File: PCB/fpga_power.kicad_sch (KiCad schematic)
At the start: 11 parts, among them U2 LFE5U-25F-6BG256C

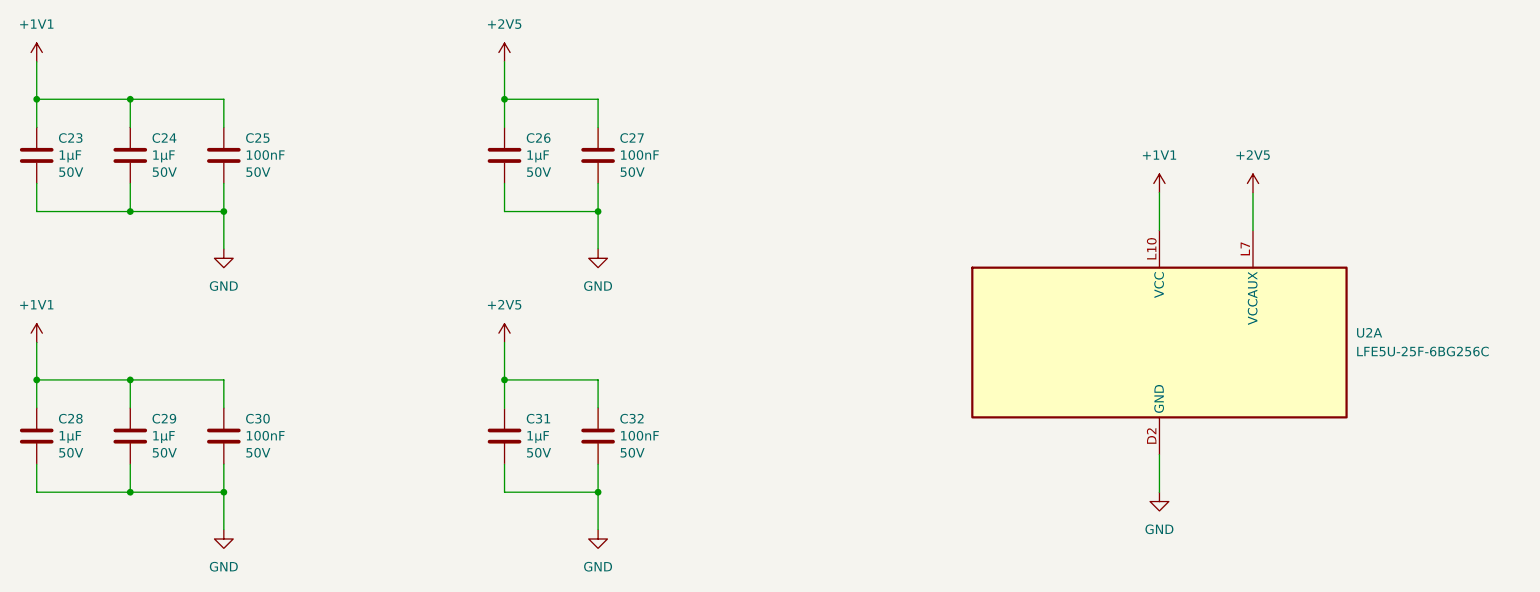
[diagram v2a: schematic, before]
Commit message: Add the USB to JTAG bridge
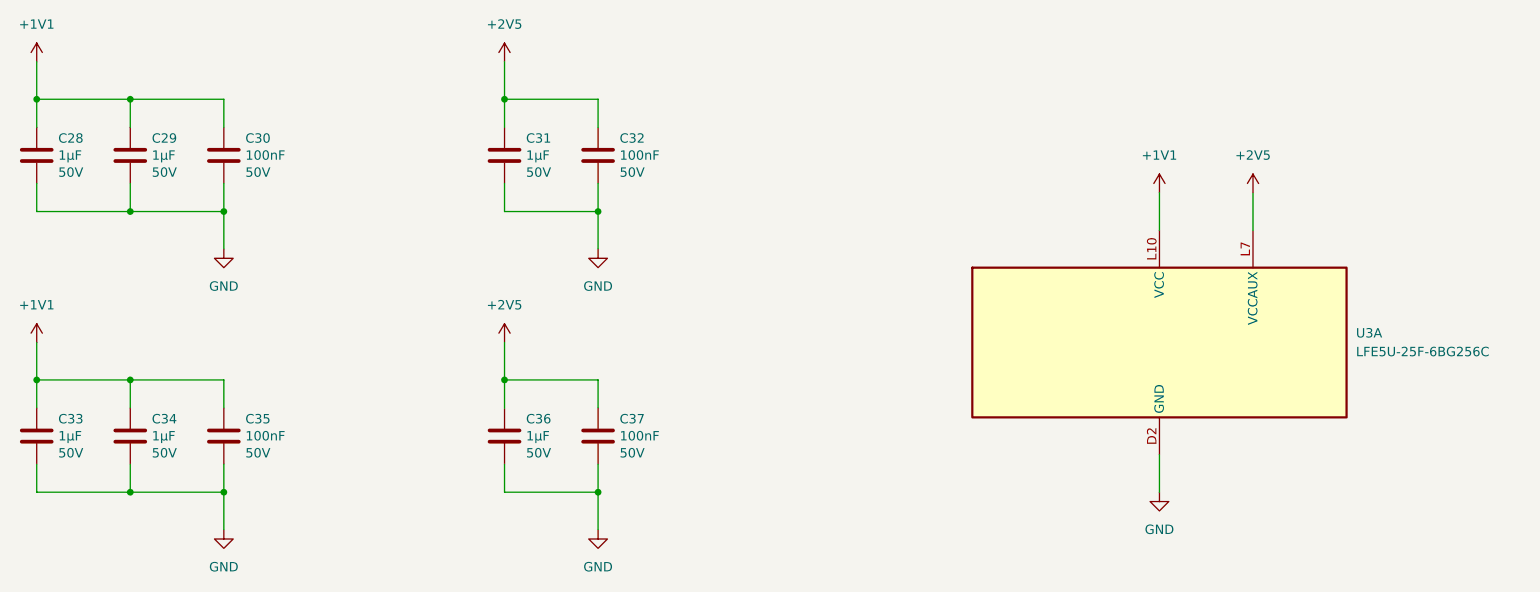
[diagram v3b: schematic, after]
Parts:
- renumbered C23 to C28, C24 to C29, C25 to C30, C26 to C31, C27 to C32, C28 to C33, C29 to C34, C30 to C35, C31 to C36, C32 to C37, U2 to U3
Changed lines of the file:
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@@
 		(on_board yes)
 		(dnp no)
-		(property "Reference" "C23"
+		(property "Reference" "C28"
 			(at 53.721 61.1886 0)
 			(effects
@@
 			(project "clavier"
 				(path "/6362c6e0-59ef-40d3-b6e0-7e9dfe7b9b20/d73938da-f0ba-48e3-aac9-a36988c25c2c/e36c52fe-7af8-49a0-bf3c-a636c30fc9cb"
-					(reference "C23")
+					(reference "C28")
 					(unit 1)
 				)
@@
 		(on_board yes)
 		(dnp no)
-		(property "Reference" "C25"
+		(property "Reference" "C30"
 			(at 79.121 61.1886 0)
 			(effects
@@
 			(project "clavier"
 				(path "/6362c6e0-59ef-40d3-b6e0-7e9dfe7b9b20/d73938da-f0ba-48e3-aac9-a36988c25c2c/e36c52fe-7af8-49a0-bf3c-a636c30fc9cb"
-					(reference "C25")
+					(reference "C30")
 					(unit 1)
 				)
@@
 		(on_board yes)
 		(dnp no)
-		(property "Reference" "C24"
+		(property "Reference" "C29"
 			(at 66.421 61.1886 0)
 			(effects
@@
 			(project "clavier"
 				(path "/6362c6e0-59ef-40d3-b6e0-7e9dfe7b9b20/d73938da-f0ba-48e3-aac9-a36988c25c2c/e36c52fe-7af8-49a0-bf3c-a636c30fc9cb"
-					(reference "C24")
+					(reference "C29")
 					(unit 1)
 				)
@@
 		(on_board yes)
 		(dnp no)
-		(property "Reference" "C29"
+		(property "Reference" "C34"
 			(at 66.421 99.2886 0)
 			(effects
@@
 			(project "clavier"
 				(path "/6362c6e0-59ef-40d3-b6e0-7e9dfe7b9b20/d73938da-f0ba-48e3-aac9-a36988c25c2c/e36c52fe-7af8-49a0-bf3c-a636c30fc9cb"
-					(reference "C29")
+					(reference "C34")
 					(unit 1)
 				)
@@
 		(on_board yes)
 		(dnp no)
-		(property "Reference" "C31"
+		(property "Reference" "C36"
 			(at 117.221 99.2886 0)
 			(effects
@@
 			(project "clavier"
 				(path "/6362c6e0-59ef-40d3-b6e0-7e9dfe7b9b20/d73938da-f0ba-48e3-aac9-a36988c25c2c/e36c52fe-7af8-49a0-bf3c-a636c30fc9cb"
-					(reference "C31")
+					(reference "C36")
 					(unit 1)
 				)
@@
 		(on_board yes)
 		(dnp no)
-		(property "Reference" "C26"
+		(property "Reference" "C31"
 			(at 117.221 61.1886 0)
 			(effects
@@
 			(project "clavier"
 				(path "/6362c6e0-59ef-40d3-b6e0-7e9dfe7b9b20/d73938da-f0ba-48e3-aac9-a36988c25c2c/e36c52fe-7af8-49a0-bf3c-a636c30fc9cb"
-					(reference "C26")
+					(reference "C31")
 					(unit 1)
 				)
@@
 		(dnp no)
 		(fields_autoplaced yes)
-		(property "Reference" "U2"
+		(property "Reference" "U3"
 			(at 229.87 87.6299 0)
 			(effects
@@
 			(project "clavier"
 				(path "/6362c6e0-59ef-40d3-b6e0-7e9dfe7b9b20/d73938da-f0ba-48e3-aac9-a36988c25c2c/e36c52fe-7af8-49a0-bf3c-a636c30fc9cb"
-					(reference "U2")
+					(reference "U3")
 					(unit 1)
 				)
@@
 		(dnp no)
 		(fields_autoplaced yes)
-		(property "Reference" "#PWR044"
+		(property "Reference" "#PWR054"
 			(at 114.3 54.61 0)
 			(effects
@@
 			(project "clavier"
 				(path "/6362c6e0-59ef-40d3-b6e0-7e9dfe7b9b20/d73938da-f0ba-48e3-aac9-a36988c25c2c/e36c52fe-7af8-49a0-bf3c-a636c30fc9cb"
-					(reference "#PWR044")
+					(reference "#PWR054")
 					(unit 1)
 				)
@@
 		(on_board yes)
 		(dnp no)
-		(property "Reference" "C32"
+		(property "Reference" "C37"
 			(at 129.921 99.2886 0)
 			(effects
@@
 			(project "clavier"
 				(path "/6362c6e0-59ef-40d3-b6e0-7e9dfe7b9b20/d73938da-f0ba-48e3-aac9-a36988c25c2c/e36c52fe-7af8-49a0-bf3c-a636c30fc9cb"
-					(reference "C32")
+					(reference "C37")
 					(unit 1)
 				)
@@
 		(dnp no)
 		(fields_autoplaced yes)
-		(property "Reference" "#PWR053"
+		(property "Reference" "#PWR063"
 			(at 127 120.65 0)
 			(effects
@@
 			(project "clavier"
 				(path "/6362c6e0-59ef-40d3-b6e0-7e9dfe7b9b20/d73938da-f0ba-48e3-aac9-a36988c25c2c/e36c52fe-7af8-49a0-bf3c-a636c30fc9cb"
-					(reference "#PWR053")
+					(reference "#PWR063")
 					(unit 1)
 				)
@@
 		(dnp no)
 		(fields_autoplaced yes)
-		(property "Reference" "#PWR046"
+		(property "Reference" "#PWR056"
 			(at 215.9 72.39 0)
 			(effects
@@
 			(project "clavier"
 				(path "/6362c6e0-59ef-40d3-b6e0-7e9dfe7b9b20/d73938da-f0ba-48e3-aac9-a36988c25c2c/e36c52fe-7af8-49a0-bf3c-a636c30fc9cb"
-					(reference "#PWR046")
+					(reference "#PWR056")
 					(unit 1)
 				)
@@
 		(dnp no)
 		(fields_autoplaced yes)
-		(property "Reference" "#PWR045"
+		(property "Reference" "#PWR055"
 			(at 203.2 72.39 0)
 			(effects
@@
 			(project "clavier"
 				(path "/6362c6e0-59ef-40d3-b6e0-7e9dfe7b9b20/d73938da-f0ba-48e3-aac9-a36988c25c2c/e36c52fe-7af8-49a0-bf3c-a636c30fc9cb"
-					(reference "#PWR045")
+					(reference "#PWR055")
 					(unit 1)
 				)
@@
 		(dnp no)
 		(fields_autoplaced yes)
-		(property "Reference" "#PWR048"
+		(property "Reference" "#PWR058"
 			(at 127 82.55 0)
 			(effects
@@
 			(project "clavier"
 				(path "/6362c6e0-59ef-40d3-b6e0-7e9dfe7b9b20/d73938da-f0ba-48e3-aac9-a36988c25c2c/e36c52fe-7af8-49a0-bf3c-a636c30fc9cb"
-					(reference "#PWR048")
+					(reference "#PWR058")
 					(unit 1)
 				)
@@
 		(dnp no)
 		(fields_autoplaced yes)
-		(property "Reference" "#PWR047"
+		(property "Reference" "#PWR057"
 			(at 76.2 82.55 0)
 			(effects
@@
 			(project "clavier"
 				(path "/6362c6e0-59ef-40d3-b6e0-7e9dfe7b9b20/d73938da-f0ba-48e3-aac9-a36988c25c2c/e36c52fe-7af8-49a0-bf3c-a636c30fc9cb"
-					(reference "#PWR047")
+					(reference "#PWR057")
 					(unit 1)
 				)
@@
 		(dnp no)
 		(fields_autoplaced yes)
-		(property "Reference" "#PWR043"
+		(property "Reference" "#PWR053"
 			(at 50.8 54.61 0)
 			(effects
@@
 			(project "clavier"
 				(path "/6362c6e0-59ef-40d3-b6e0-7e9dfe7b9b20/d73938da-f0ba-48e3-aac9-a36988c25c2c/e36c52fe-7af8-49a0-bf3c-a636c30fc9cb"
-					(reference "#PWR043")
+					(reference "#PWR053")
 					(unit 1)
 				)
@@
 		(on_board yes)
 		(dnp no)
-		(property "Reference" "C28"
+		(property "Reference" "C33"
 			(at 53.721 99.2886 0)
 			(effects
@@
 			(project "clavier"
 				(path "/6362c6e0-59ef-40d3-b6e0-7e9dfe7b9b20/d73938da-f0ba-48e3-aac9-a36988c25c2c/e36c52fe-7af8-49a0-bf3c-a636c30fc9cb"
-					(reference "C28")
+					(reference "C33")
 					(unit 1)
 				)
@@
 		(dnp no)
 		(fields_autoplaced yes)
-		(property "Reference" "#PWR051"
+		(property "Reference" "#PWR061"
 			(at 203.2 115.57 0)
 			(effects
@@
 			(project "clavier"
 				(path "/6362c6e0-59ef-40d3-b6e0-7e9dfe7b9b20/d73938da-f0ba-48e3-aac9-a36988c25c2c/e36c52fe-7af8-49a0-bf3c-a636c30fc9cb"
-					(reference "#PWR051")
+					(reference "#PWR061")
 					(unit 1)
 				)
@@
 		(dnp no)
 		(fields_autoplaced yes)
-		(property "Reference" "#PWR049"
+		(property "Reference" "#PWR059"
 			(at 50.8 92.71 0)
 			(effects
@@
 			(project "clavier"
 				(path "/6362c6e0-59ef-40d3-b6e0-7e9dfe7b9b20/d73938da-f0ba-48e3-aac9-a36988c25c2c/e36c52fe-7af8-49a0-bf3c-a636c30fc9cb"
-					(reference "#PWR049")
+					(reference "#PWR059")
 					(unit 1)
 				)
@@
 		(on_board yes)
 		(dnp no)
-		(property "Reference" "C27"
+		(property "Reference" "C32"
 			(at 129.921 61.1886 0)
 			(effects
@@
 			(project "clavier"
 				(path "/6362c6e0-59ef-40d3-b6e0-7e9dfe7b9b20/d73938da-f0ba-48e3-aac9-a36988c25c2c/e36c52fe-7af8-49a0-bf3c-a636c30fc9cb"
-					(reference "C27")
+					(reference "C32")
 					(unit 1)
 				)
@@
 		(dnp no)
 		(fields_autoplaced yes)
-		(property "Reference" "#PWR050"
+		(property "Reference" "#PWR060"
 			(at 114.3 92.71 0)
 			(effects
@@
 			(project "clavier"
 				(path "/6362c6e0-59ef-40d3-b6e0-7e9dfe7b9b20/d73938da-f0ba-48e3-aac9-a36988c25c2c/e36c52fe-7af8-49a0-bf3c-a636c30fc9cb"
-					(reference "#PWR050")
+					(reference "#PWR060")
 					(unit 1)
 				)
@@
 		(dnp no)
 		(fields_autoplaced yes)
-		(property "Reference" "#PWR052"
+		(property "Reference" "#PWR062"
 			(at 76.2 120.65 0)
 			(effects
@@
 			(project "clavier"
 				(path "/6362c6e0-59ef-40d3-b6e0-7e9dfe7b9b20/d73938da-f0ba-48e3-aac9-a36988c25c2c/e36c52fe-7af8-49a0-bf3c-a636c30fc9cb"
-					(reference "#PWR052")
+					(reference "#PWR062")
 					(unit 1)
 				)
@@
 		(on_board yes)
 		(dnp no)
-		(property "Reference" "C30"
+		(property "Reference" "C35"
 			(at 79.121 99.2886 0)
 			(effects
@@
 			(project "clavier"
 				(path "/6362c6e0-59ef-40d3-b6e0-7e9dfe7b9b20/d73938da-f0ba-48e3-aac9-a36988c25c2c/e36c52fe-7af8-49a0-bf3c-a636c30fc9cb"
-					(reference "C30")
+					(reference "C35")
 					(unit 1)
 				)

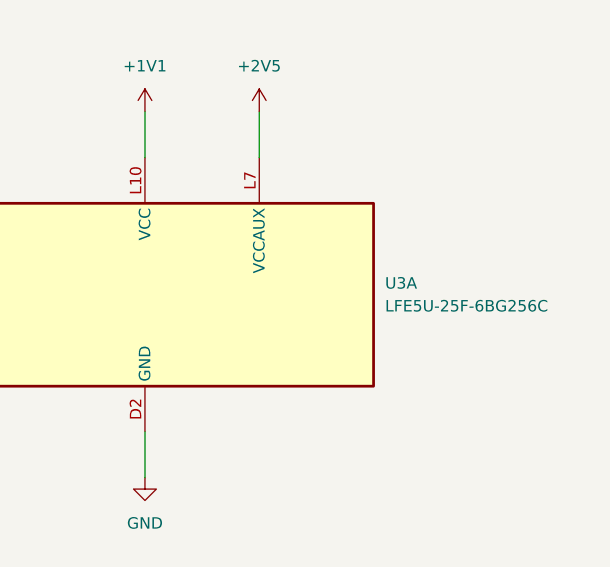
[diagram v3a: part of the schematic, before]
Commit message: Improve the CH347F schematics and added 3D models
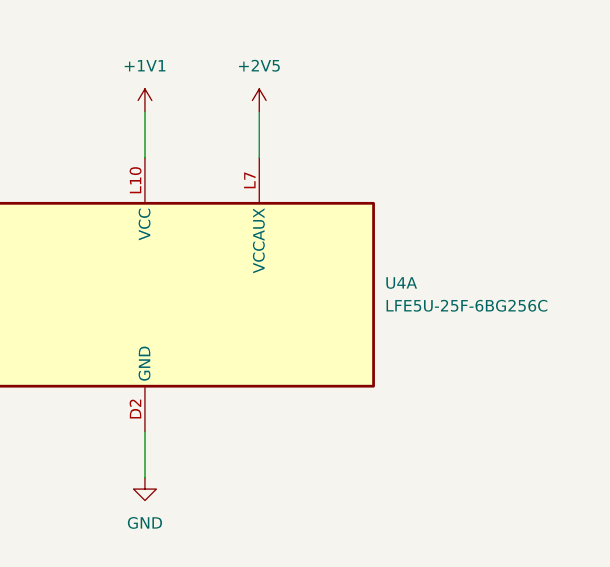
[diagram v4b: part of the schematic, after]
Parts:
- renumbered U3 to U4
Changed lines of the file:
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@@
 		(dnp no)
 		(fields_autoplaced yes)
-		(property "Reference" "U3"
+		(property "Reference" "U4"
 			(at 229.87 87.6299 0)
 			(effects
@@
 			(project "clavier"
 				(path "/6362c6e0-59ef-40d3-b6e0-7e9dfe7b9b20/d73938da-f0ba-48e3-aac9-a36988c25c2c/e36c52fe-7af8-49a0-bf3c-a636c30fc9cb"
-					(reference "U3")
+					(reference "U4")
 					(unit 1)
 				)
@@
 		(dnp no)
 		(fields_autoplaced yes)
-		(property "Reference" "#PWR054"
+		(property "Reference" "#PWR058"
 			(at 114.3 54.61 0)
 			(effects
@@
 			(project "clavier"
 				(path "/6362c6e0-59ef-40d3-b6e0-7e9dfe7b9b20/d73938da-f0ba-48e3-aac9-a36988c25c2c/e36c52fe-7af8-49a0-bf3c-a636c30fc9cb"
-					(reference "#PWR054")
+					(reference "#PWR058")
 					(unit 1)
 				)
@@
 		(dnp no)
 		(fields_autoplaced yes)
-		(property "Reference" "#PWR063"
+		(property "Reference" "#PWR067"
 			(at 127 120.65 0)
 			(effects
@@
 			(project "clavier"
 				(path "/6362c6e0-59ef-40d3-b6e0-7e9dfe7b9b20/d73938da-f0ba-48e3-aac9-a36988c25c2c/e36c52fe-7af8-49a0-bf3c-a636c30fc9cb"
-					(reference "#PWR063")
+					(reference "#PWR067")
 					(unit 1)
 				)
@@
 		(dnp no)
 		(fields_autoplaced yes)
-		(property "Reference" "#PWR056"
+		(property "Reference" "#PWR060"
 			(at 215.9 72.39 0)
 			(effects
@@
 			(project "clavier"
 				(path "/6362c6e0-59ef-40d3-b6e0-7e9dfe7b9b20/d73938da-f0ba-48e3-aac9-a36988c25c2c/e36c52fe-7af8-49a0-bf3c-a636c30fc9cb"
-					(reference "#PWR056")
+					(reference "#PWR060")
 					(unit 1)
 				)
@@
 		(dnp no)
 		(fields_autoplaced yes)
-		(property "Reference" "#PWR055"
+		(property "Reference" "#PWR059"
 			(at 203.2 72.39 0)
 			(effects
@@
 			(project "clavier"
 				(path "/6362c6e0-59ef-40d3-b6e0-7e9dfe7b9b20/d73938da-f0ba-48e3-aac9-a36988c25c2c/e36c52fe-7af8-49a0-bf3c-a636c30fc9cb"
-					(reference "#PWR055")
+					(reference "#PWR059")
 					(unit 1)
 				)
@@
 		(dnp no)
 		(fields_autoplaced yes)
-		(property "Reference" "#PWR058"
+		(property "Reference" "#PWR062"
 			(at 127 82.55 0)
 			(effects
@@
 			(project "clavier"
 				(path "/6362c6e0-59ef-40d3-b6e0-7e9dfe7b9b20/d73938da-f0ba-48e3-aac9-a36988c25c2c/e36c52fe-7af8-49a0-bf3c-a636c30fc9cb"
-					(reference "#PWR058")
+					(reference "#PWR062")
 					(unit 1)
 				)
@@
 		(dnp no)
 		(fields_autoplaced yes)
-		(property "Reference" "#PWR057"
+		(property "Reference" "#PWR061"
 			(at 76.2 82.55 0)
 			(effects
@@
 			(project "clavier"
 				(path "/6362c6e0-59ef-40d3-b6e0-7e9dfe7b9b20/d73938da-f0ba-48e3-aac9-a36988c25c2c/e36c52fe-7af8-49a0-bf3c-a636c30fc9cb"
-					(reference "#PWR057")
+					(reference "#PWR061")
 					(unit 1)
 				)
@@
 		(dnp no)
 		(fields_autoplaced yes)
-		(property "Reference" "#PWR053"
+		(property "Reference" "#PWR057"
 			(at 50.8 54.61 0)
 			(effects
@@
 			(project "clavier"
 				(path "/6362c6e0-59ef-40d3-b6e0-7e9dfe7b9b20/d73938da-f0ba-48e3-aac9-a36988c25c2c/e36c52fe-7af8-49a0-bf3c-a636c30fc9cb"
-					(reference "#PWR053")
+					(reference "#PWR057")
 					(unit 1)
 				)
@@
 		(dnp no)
 		(fields_autoplaced yes)
-		(property "Reference" "#PWR061"
+		(property "Reference" "#PWR065"
 			(at 203.2 115.57 0)
 			(effects
@@
 			(project "clavier"
 				(path "/6362c6e0-59ef-40d3-b6e0-7e9dfe7b9b20/d73938da-f0ba-48e3-aac9-a36988c25c2c/e36c52fe-7af8-49a0-bf3c-a636c30fc9cb"
-					(reference "#PWR061")
+					(reference "#PWR065")
 					(unit 1)
 				)
@@
 		(dnp no)
 		(fields_autoplaced yes)
-		(property "Reference" "#PWR059"
+		(property "Reference" "#PWR063"
 			(at 50.8 92.71 0)
 			(effects
@@
 			(project "clavier"
 				(path "/6362c6e0-59ef-40d3-b6e0-7e9dfe7b9b20/d73938da-f0ba-48e3-aac9-a36988c25c2c/e36c52fe-7af8-49a0-bf3c-a636c30fc9cb"
-					(reference "#PWR059")
+					(reference "#PWR063")
 					(unit 1)
 				)
@@
 		(dnp no)
 		(fields_autoplaced yes)
-		(property "Reference" "#PWR060"
+		(property "Reference" "#PWR064"
 			(at 114.3 92.71 0)
 			(effects
@@
 			(project "clavier"
 				(path "/6362c6e0-59ef-40d3-b6e0-7e9dfe7b9b20/d73938da-f0ba-48e3-aac9-a36988c25c2c/e36c52fe-7af8-49a0-bf3c-a636c30fc9cb"
-					(reference "#PWR060")
+					(reference "#PWR064")
 					(unit 1)
 				)
@@
 		(dnp no)
 		(fields_autoplaced yes)
-		(property "Reference" "#PWR062"
+		(property "Reference" "#PWR066"
 			(at 76.2 120.65 0)
 			(effects
@@
 			(project "clavier"
 				(path "/6362c6e0-59ef-40d3-b6e0-7e9dfe7b9b20/d73938da-f0ba-48e3-aac9-a36988c25c2c/e36c52fe-7af8-49a0-bf3c-a636c30fc9cb"
-					(reference "#PWR062")
+					(reference "#PWR066")
 					(unit 1)
 				)
